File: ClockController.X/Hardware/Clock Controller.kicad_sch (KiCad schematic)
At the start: 3 parts

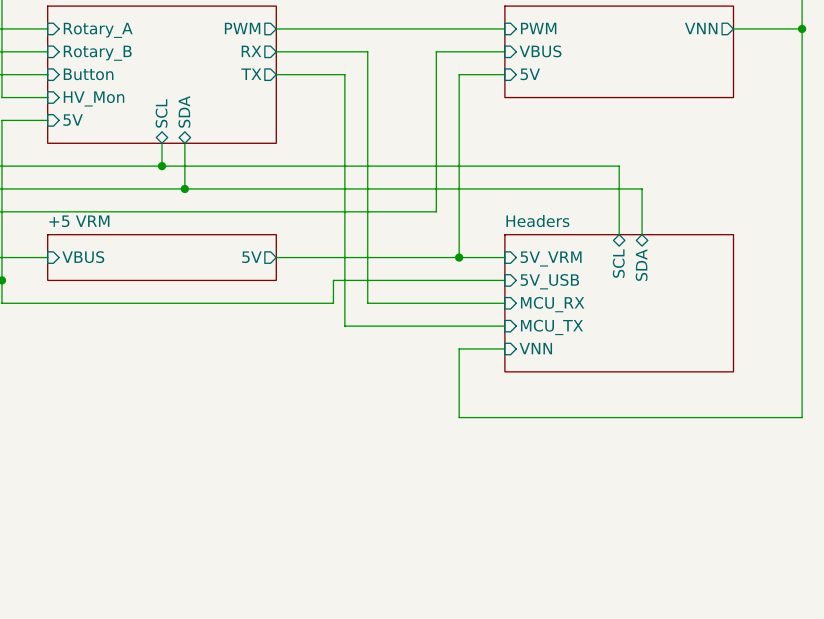
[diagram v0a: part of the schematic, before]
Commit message: Added RTC and battery to schematic
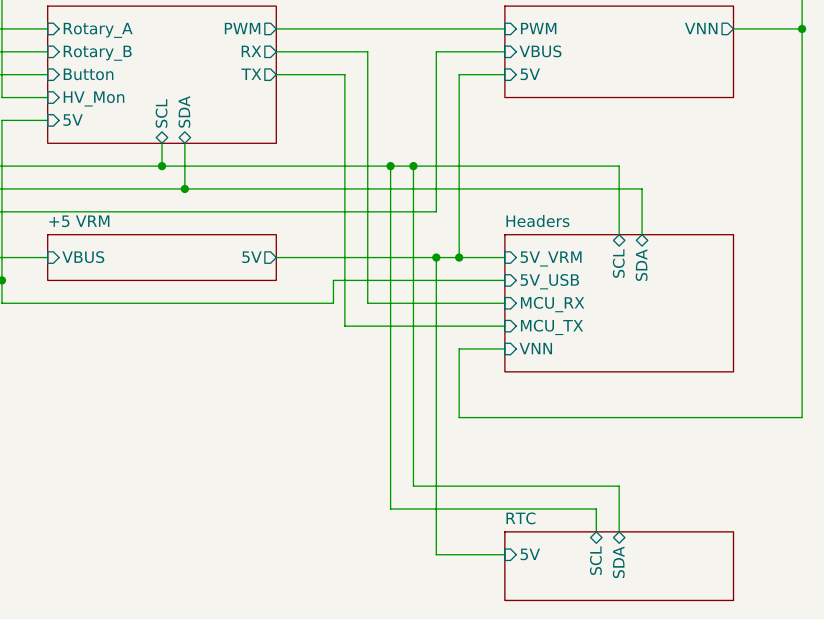
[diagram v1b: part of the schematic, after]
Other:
- added sheet RTC (rtc.kicad_sch)
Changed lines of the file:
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@@
+	)
+	(junction
+		(at 167.64 68.58)
+		(diameter 0)
+		(color 0 0 0 0)
 	)
 	(junction
@@
 	)
 	(junction
+		(at 165.1 68.58)
+		(diameter 0)
+		(color 0 0 0 0)
+	)
+	(junction
 		(at 121.92 81.28)
 		(diameter 0)
 		(color 0 0 0 0)
 	)
+	(junction
+		(at 170.18 78.74)
+		(diameter 0)
+		(color 0 0 0 0)
+	)
 	(wire
 		(pts
@@
 	(wire
 		(pts
+			(xy 165.1 68.58) (xy 167.64 68.58)
+		)
+		(stroke
+			(width 0)
+			(type default)
+		)
+	)
+	(wire
+		(pts
 			(xy 121.92 45.72) (xy 121.92 60.96)
 		)
@@
 	(wire
 		(pts
+			(xy 187.96 106.68) (xy 165.1 106.68)
+		)
+		(stroke
+			(width 0)
+			(type default)
+		)
+	)
+	(wire
+		(pts
 			(xy 160.02 58.42) (xy 160.02 86.36)
 		)
@@
 	(wire
 		(pts
+			(xy 177.8 111.76) (xy 170.18 111.76)
+		)
+		(stroke
+			(width 0)
+			(type default)
+		)
+	)
+	(wire
+		(pts
 			(xy 142.24 66.04) (xy 142.24 71.12)
 		)
@@
 	(wire
 		(pts
+			(xy 165.1 106.68) (xy 165.1 68.58)
+		)
+		(stroke
+			(width 0)
+			(type default)
+		)
+	)
+	(wire
+		(pts
 			(xy 101.6 78.74) (xy 106.68 78.74)
 		)
@@
 	(wire
 		(pts
-			(xy 152.4 78.74) (xy 172.72 78.74)
+			(xy 190.5 109.22) (xy 190.5 104.14)
+		)
+		(stroke
+			(width 0)
+			(type default)
+		)
+	)
+	(wire
+		(pts
+			(xy 152.4 78.74) (xy 170.18 78.74)
 		)
 		(stroke
@@
 	(wire
 		(pts
+			(xy 167.64 104.14) (xy 167.64 68.58)
+		)
+		(stroke
+			(width 0)
+			(type default)
+		)
+	)
+	(wire
+		(pts
+			(xy 170.18 111.76) (xy 170.18 78.74)
+		)
+		(stroke
+			(width 0)
+			(type default)
+		)
+	)
+	(wire
+		(pts
+			(xy 167.64 68.58) (xy 190.5 68.58)
+		)
+		(stroke
+			(width 0)
+			(type default)
+		)
+	)
+	(wire
+		(pts
 			(xy 101.6 55.88) (xy 127 55.88)
 		)
@@
 	(wire
 		(pts
+			(xy 170.18 78.74) (xy 172.72 78.74)
+		)
+		(stroke
+			(width 0)
+			(type default)
+		)
+	)
+	(wire
+		(pts
 			(xy 170.18 73.66) (xy 106.68 73.66)
 		)
@@
 	(wire
 		(pts
-			(xy 139.7 68.58) (xy 190.5 68.58)
+			(xy 139.7 68.58) (xy 165.1 68.58)
 		)
 		(stroke
@@
 	(wire
 		(pts
+			(xy 190.5 104.14) (xy 167.64 104.14)
+		)
+		(stroke
+			(width 0)
+			(type default)
+		)
+	)
+	(wire
+		(pts
 			(xy 88.9 68.58) (xy 88.9 76.2)
+		)
+		(stroke
+			(width 0)
+			(type default)
+		)
+	)
+	(wire
+		(pts
+			(xy 187.96 109.22) (xy 187.96 106.68)
 		)
 		(stroke
@@
 				)
 			)
+		)
+	)
+	(sheet
+		(at 177.8 109.22)
+		(size 25.4 7.62)
+		(exclude_from_sim no)
+		(in_bom yes)
+		(on_board yes)
+		(dnp no)
+		(fields_autoplaced yes)
+		(stroke
+			(width 0.1524)
+			(type solid)
+		)
+		(fill
+			(color 0 0 0 0.0000)
+		)
+		(property "Sheetname" "RTC"
+			(at 177.8 108.5084 0)
+			(effects
+				(font
+					(size 1.27 1.27)
+				)
+				(justify left bottom)
+			)
+		)
+		(property "Sheetfile" "rtc.kicad_sch"
+			(at 177.8 117.4246 0)
+			(effects
+				(font
+					(size 1.27 1.27)
+				)
+				(justify left top)
+				(hide yes)
+			)
+		)
+		(pin "5V" input
+			(at 177.8 111.76 180)
+			(effects
+				(font
+					(size 1.27 1.27)
+				)
+				(justify left)
+			)
+		)
+		(pin "SCL" bidirectional
+			(at 187.96 109.22 90)
+			(effects
+				(font
+					(size 1.27 1.27)
+				)
+				(justify right)
+			)
+		)
+		(pin "SDA" bidirectional
+			(at 190.5 109.22 90)
+			(effects
+				(font
+					(size 1.27 1.27)
+				)
+				(justify right)
+			)
+		)
+		(instances
+			(project "Clock Controller"
+				(path "/de4049ea-1674-4dcc-86d3-bb1be3dcf2e7"
+					(page "9")
+				)
+			)

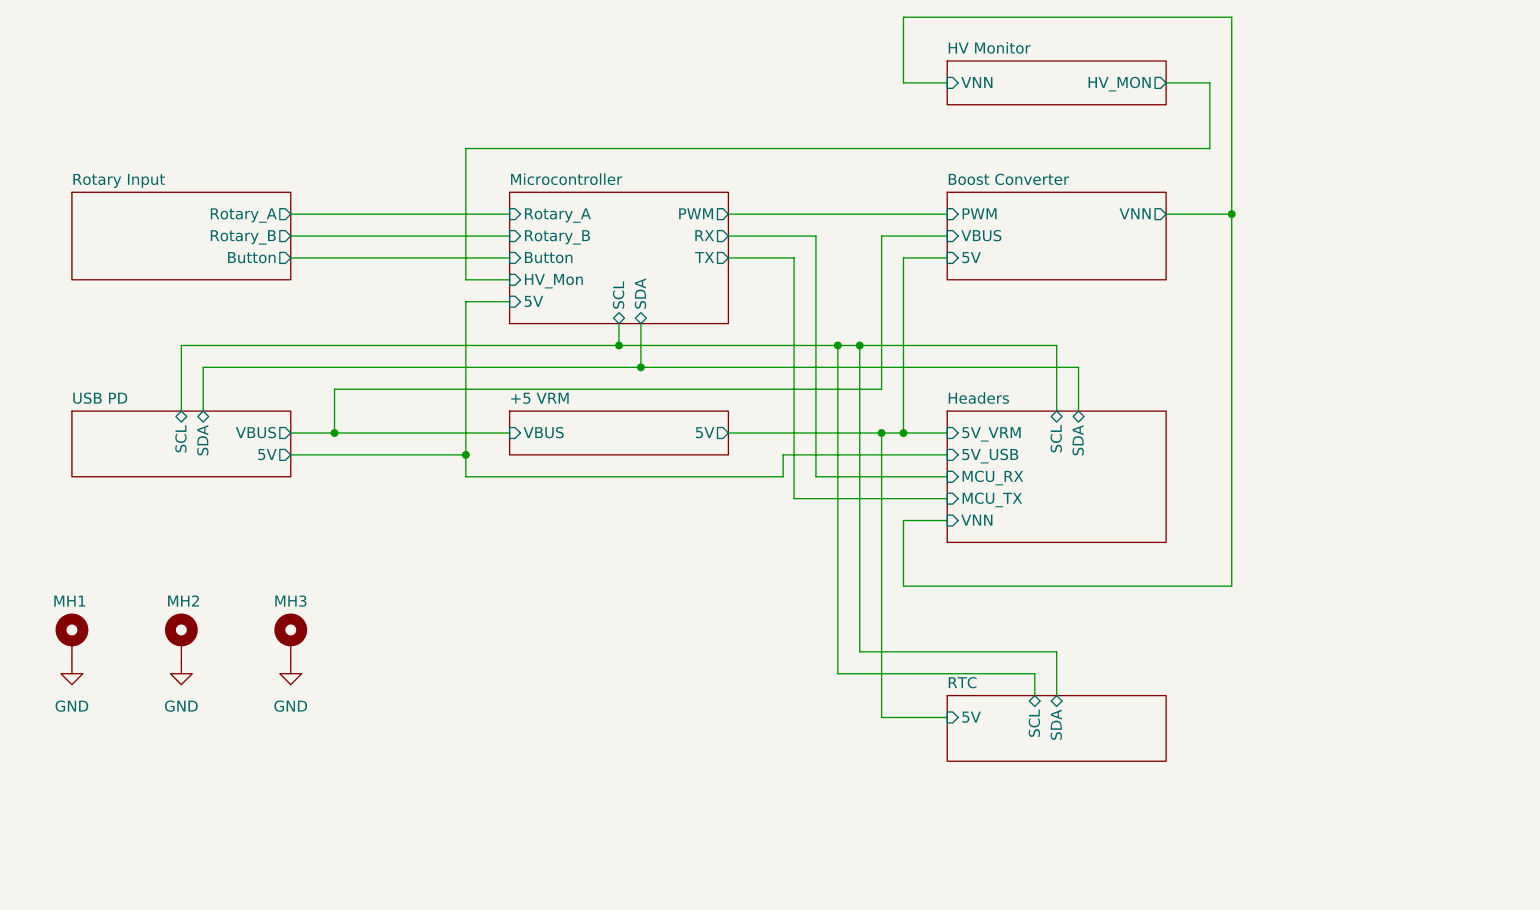
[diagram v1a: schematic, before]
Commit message: Converting to single board layout
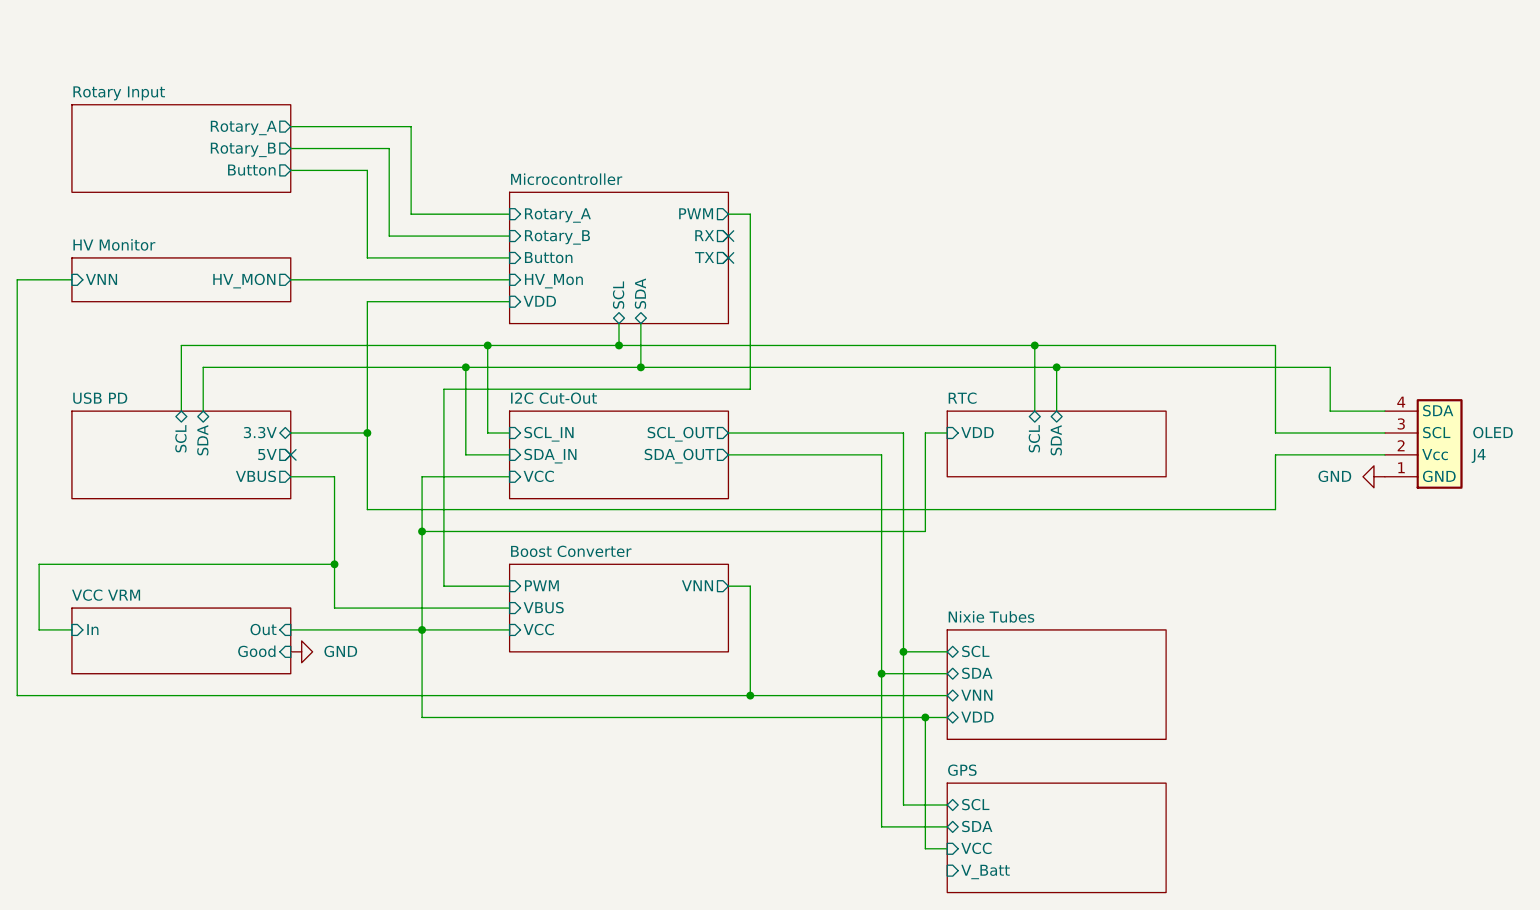
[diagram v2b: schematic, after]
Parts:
- removed MH1, MH2, MH3: M2.5_MTGP540H285, MountingHole:MountingHole_2.5mm_Pad, symbol Mechanical:MountingHole_Pad
- added J4: OLED, Display_:SSD1306 0.91 128x32 OLED, symbol Display_:SSD1306
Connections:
- net GND: now also J4.1 (GND)
- new net I2C Cut-Out/SCL_IN: J4.3 (SCL)
- new net I2C Cut-Out/SDA_IN: J4.4 (SDA)
- new net Microcontroller/VDD: J4.2 (Vcc)
- no-connect marks 0 -> 3
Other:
- removed sheet +5 VRM
- removed sheet Headers
- added sheet GPS (GPS.kicad_sch)
- added sheet I2C Cut-Out (I2C Cut-Out.kicad_sch)
- added sheet Nixie Tubes (Nixie Tubes.kicad_sch)
- added sheet VCC VRM (VCC VRM.kicad_sch)
- sheet Boost Converter ports: added VCC; removed 5V
- sheet Microcontroller ports: added VDD; removed 5V
- sheet RTC ports: added VDD; removed 5V
- sheet USB PD ports: added 3.3V; removed none
